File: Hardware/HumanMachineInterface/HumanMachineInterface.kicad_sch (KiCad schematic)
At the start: 18 parts, among them Q1 Q_Photo_NPN, SW1 SW_Push, SW2 SW_Push, SW3 SW_Push, SW4 SW_Push, U2 ST7735S

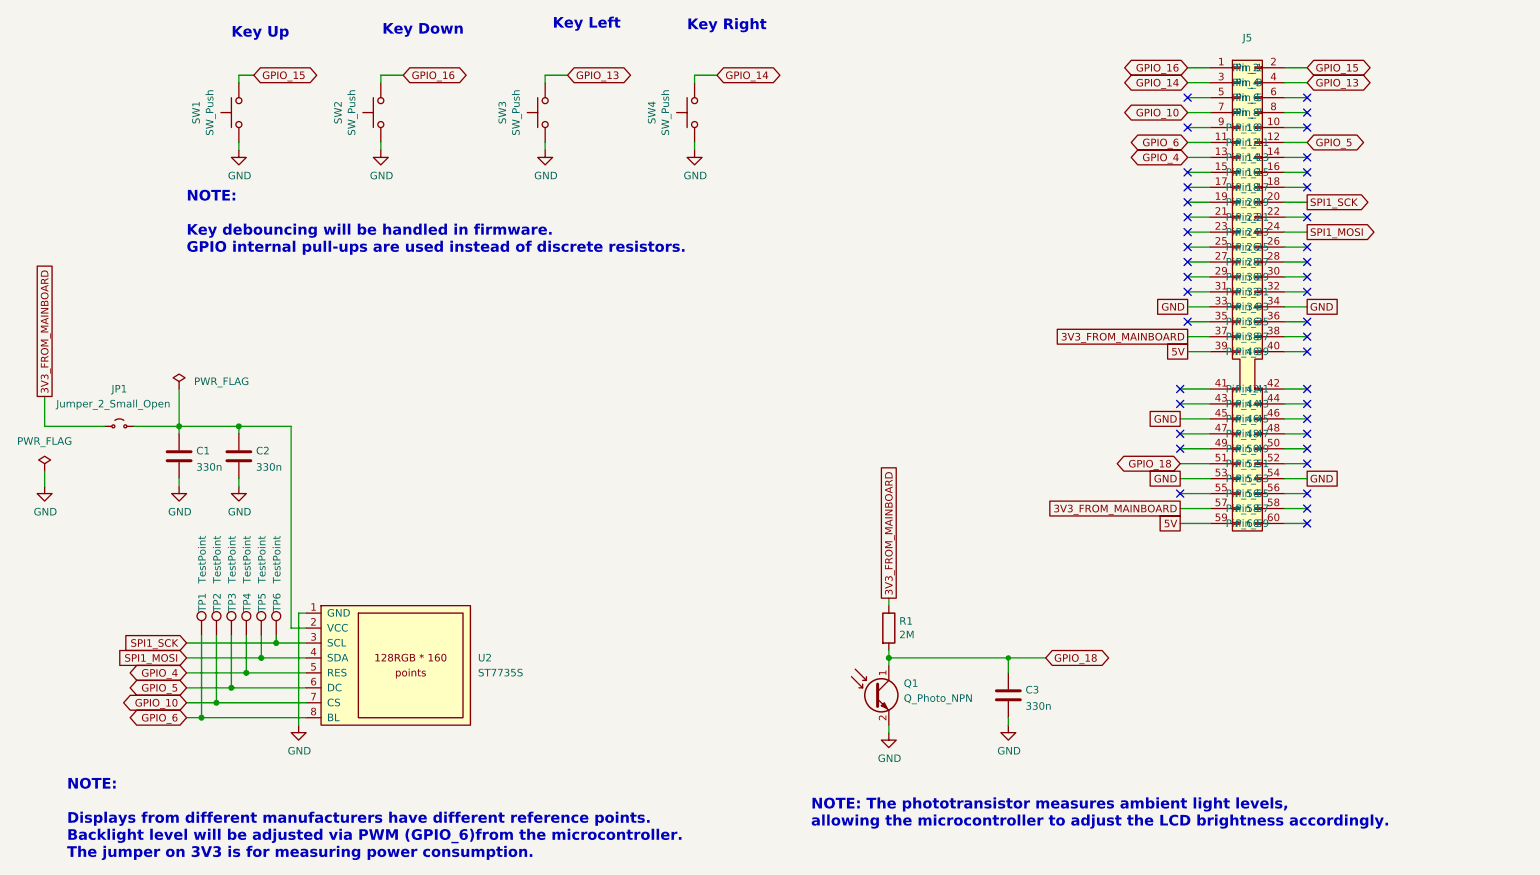
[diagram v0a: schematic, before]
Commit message: rework CI, make PCB smaller
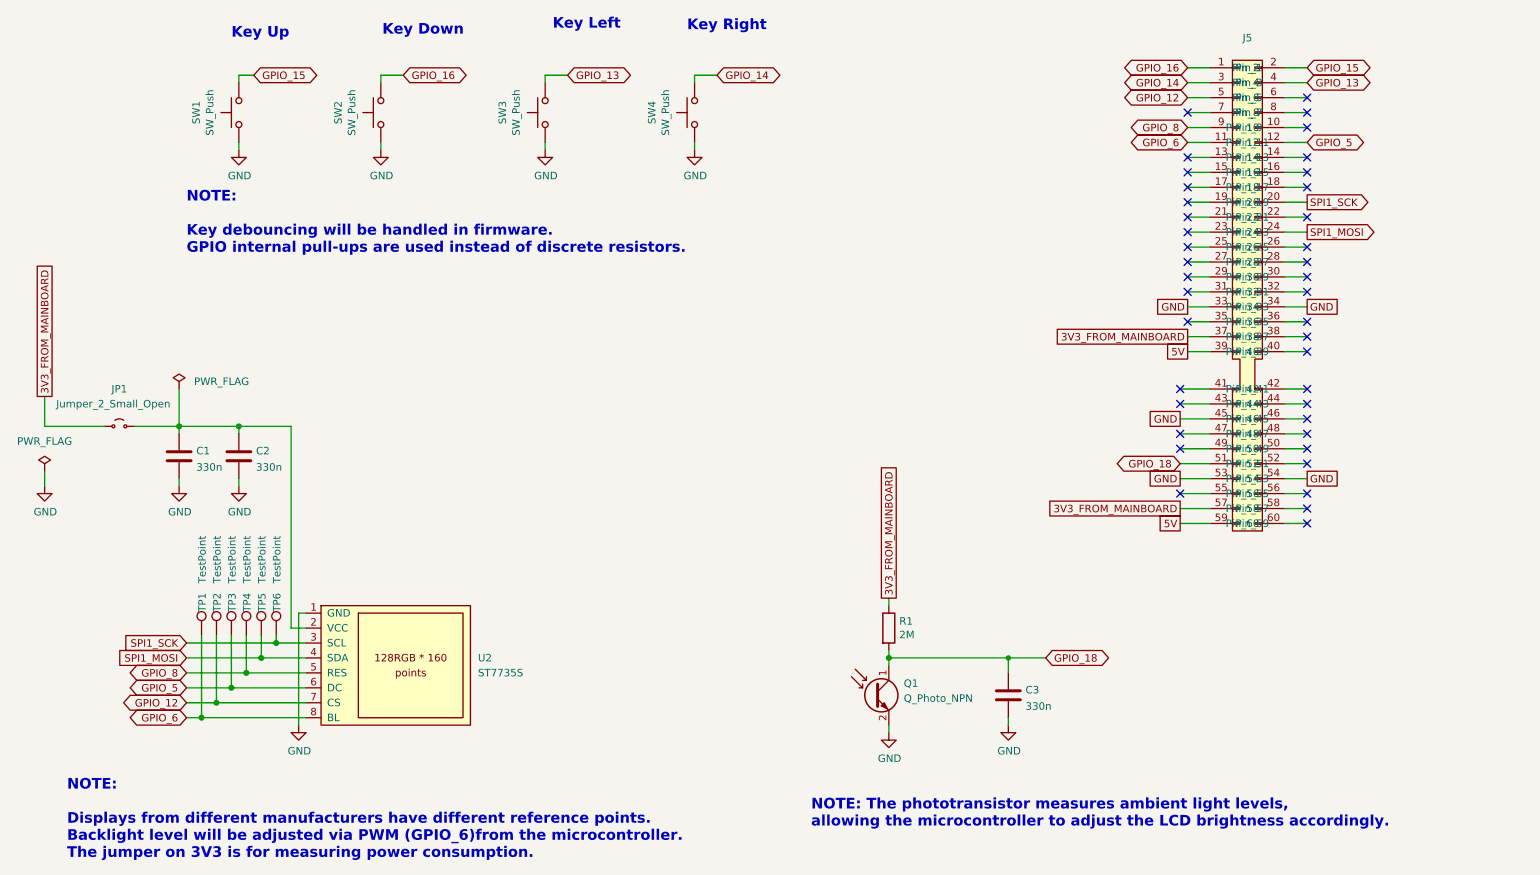
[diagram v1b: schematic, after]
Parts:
- SW1, SW2, SW3, SW4: footprint Button_Switch_SMD:SW_SPST_PTS645 -> Button_Switch_SMD:SW_SPST_PTS645Sx43SMTR92
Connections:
- net GPIO_12: now reaches J5.5 (Pin_5)
- net GPIO_12: now also TP2.1, U2.7 (CS)
- net GPIO_8: now reaches J5.9 (Pin_9)
- net GPIO_8: now also TP4.1, U2.5 (RES)
- removed net GPIO_10: J5.7 (Pin_7), TP2.1, U2.7 (CS)
- removed net GPIO_4: J5.13 (Pin_13), TP4.1, U2.5 (RES)
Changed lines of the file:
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@@
 	)
 	(no_connect
+		(at 220.98 41.91)
+	)
+	(no_connect
 		(at 219.71 83.82)
 	)
@@
 	)
 	(no_connect
-		(at 220.98 36.83)
+		(at 219.71 91.44)
 	)
 	(no_connect
-		(at 219.71 91.44)
+		(at 220.98 34.29)
 	)
 	(no_connect
@@
 		(at 220.98 49.53)
 	)
-	(no_connect
-		(at 220.98 31.75)
-	)
 	(wire
 		(pts
@@
 		)
 	)
-	(global_label "GPIO_10"
-		(shape bidirectional)
-		(at 220.98 34.29 180)
-		(fields_autoplaced yes)
-		(effects
-			(font
-				(size 1.27 1.27)
-			)
-			(justify right)
-		)
-		(property "Intersheetrefs" "${INTERSHEET_REFS}"
-			(at 209.0216 34.29 0)
-			(effects
-				(font
-					(size 1.27 1.27)
-				)
-				(justify right)
-				(hide yes)
-			)
-		)
-	)
 	(global_label "GPIO_13"
 		(shape bidirectional)
@@
 		)
 	)
-	(global_label "GPIO_4"
-		(shape bidirectional)
-		(at 220.98 41.91 180)
-		(fields_autoplaced yes)
-		(effects
-			(font
-				(size 1.27 1.27)
-			)
-			(justify right)
-		)
-		(property "Intersheetrefs" "${INTERSHEET_REFS}"
-			(at 210.2311 41.91 0)
-			(effects
-				(font
-					(size 1.27 1.27)
-				)
-				(justify right)
-				(hide yes)
-			)
-		)
-	)
-	(global_label "GPIO_4"
+	(global_label "GPIO_8"
 		(shape bidirectional)
 		(at 50.8 129.54 180)
@@
 		)
 	)
-	(global_label "GPIO_10"
+	(global_label "GPIO_12"
 		(shape bidirectional)
 		(at 50.8 134.62 180)
@@
 		)
 	)
+	(global_label "GPIO_12"
+		(shape bidirectional)
+		(at 220.98 31.75 180)
+		(fields_autoplaced yes)
+		(effects
+			(font
+				(size 1.27 1.27)
+			)
+			(justify right)
+		)
+		(property "Intersheetrefs" "${INTERSHEET_REFS}"
+			(at 209.0216 31.75 0)
+			(effects
+				(font
+					(size 1.27 1.27)
+				)
+				(justify right)
+				(hide yes)
+			)
+		)
+	)
+	(global_label "GPIO_8"
+		(shape bidirectional)
+		(at 220.98 36.83 180)
+		(fields_autoplaced yes)
+		(effects
+			(font
+				(size 1.27 1.27)
+			)
+			(justify right)
+		)
+		(property "Intersheetrefs" "${INTERSHEET_REFS}"
+			(at 210.2311 36.83 0)
+			(effects
+				(font
+					(size 1.27 1.27)
+				)
+				(justify right)
+				(hide yes)
+			)
+		)
+	)
 	(global_label "GPIO_6"
 		(shape bidirectional)
@@
 			)
 		)
-		(property "Footprint" "Button_Switch_SMD:SW_SPST_PTS645"
+		(property "Footprint" "Button_Switch_SMD:SW_SPST_PTS645Sx43SMTR92"
 			(at 132.08 34.29 0)
 			(effects
@@
 			)
 		)
-		(property "Description" ""
+		(property "Description" "Push button switch, generic, two pins"
 			(at 137.16 34.29 0)
 			(effects
@@
 			)
 		)
-		(property "Footprint" "Button_Switch_SMD:SW_SPST_PTS645"
+		(property "Footprint" "Button_Switch_SMD:SW_SPST_PTS645Sx43SMTR92"
 			(at 78.74 34.29 0)
 			(effects
@@
 			)
 		)
-		(property "Description" ""
+		(property "Description" "Push button switch, generic, two pins"
 			(at 83.82 34.29 0)
 			(effects
@@
 			)
 		)
-		(property "Footprint" "Button_Switch_SMD:SW_SPST_PTS645"
+		(property "Footprint" "Button_Switch_SMD:SW_SPST_PTS645Sx43SMTR92"
 			(at 54.61 34.29 0)
 			(effects
@@
 			)
 		)
-		(property "Description" ""
+		(property "Description" "Push button switch, generic, two pins"
 			(at 59.69 34.29 0)
 			(effects
@@
 			)
 		)
-		(property "Footprint" "Button_Switch_SMD:SW_SPST_PTS645"
+		(property "Footprint" "Button_Switch_SMD:SW_SPST_PTS645Sx43SMTR92"
 			(at 106.68 34.29 0)
 			(effects
@@
 			)
 		)
-		(property "Description" ""
+		(property "Description" "Push button switch, generic, two pins"
 			(at 111.76 34.29 0)
 			(effects
